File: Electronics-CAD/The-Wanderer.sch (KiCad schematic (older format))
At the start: 9 parts, among them J1 Raspberry_Pi_3, M1_Left Continuous_Motor_Servo, M2_Right Continuous_Motor_Servo, U1 IR_sensor

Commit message: Fix schematic by replacing voltage divider with voltage converter
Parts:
- removed RN2: Voltage_Divider, symbol Device:Voltage_Divider
- added B1: 5V_2A_Voltage_Converter, symbol Raspberry_Pi_2_or_3:5V_2A_Voltage_Converter
- A1: symbol POE_Elias:Arduino_UNO_R3 -> The-Wanderer-rescue:Arduino_UNO_R3-POE_Elias
- J1: symbol Raspberry_Pi_2_or_3:Raspberry_Pi_3 -> The-Wanderer-rescue:Raspberry_Pi_3-Raspberry_Pi_2_or_3
- LS1: symbol Raspberry_Pi_2_or_3:Raspi_Speaker -> The-Wanderer-rescue:Raspi_Speaker-Raspberry_Pi_2_or_3
- U1: symbol Raspberry_Pi_2_or_3:IR_sensor -> The-Wanderer-rescue:IR_sensor-Raspberry_Pi_2_or_3
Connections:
- net 12V: now also B1.~
- net 5V: now also B1.~
- net GND: now also B1.~
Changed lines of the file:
@@
 $EndComp
 $Comp
-L Raspberry_Pi_2_or_3:IR_sensor U1
+L The-Wanderer-rescue:IR_sensor-Raspberry_Pi_2_or_3 U1
 U 1 1 5DF263DA
 P 3650 2350
@@
 	2200 2650 2250 2650
 $Comp
-L Device:Voltage_Divider RN2
-U 1 1 5DF46FB6
-P 4100 1500
-F 0 "RN2" V 3900 1500 50  0000 C CNN
-F 1 "Voltage_Divider" V 4000 1500 50  0000 C CNN
-F 2 "" V 4575 1500 50  0001 C CNN
-F 3 "~" H 4300 1500 50  0001 C CNN
-	1    4100 1500
-	0    1    -1   0
-$EndComp
-Text Label 4100 1200 3    50   ~ 0
-5V
-$Comp
 L power:GND #PWR?
 U 1 1 5DF4FBFA
@@
 $EndComp
 $Comp
-L Raspberry_Pi_2_or_3:Raspi_Speaker LS1
+L The-Wanderer-rescue:Raspi_Speaker-Raspberry_Pi_2_or_3 LS1
 U 1 1 5DF1BB42
 P 4400 3250
@@
 $EndComp
 $Comp
-L Raspberry_Pi_2_or_3:Raspberry_Pi_3 J1
+L The-Wanderer-rescue:Raspberry_Pi_3-Raspberry_Pi_2_or_3 J1
 U 1 1 5DF103EF
 P 5400 2450
@@
 	5200 1150 5200 900
 Wire Wire Line
-	5200 900  4100 900
-Wire Wire Line
-	4100 900  4100 1350
-Connection ~ 4100 900
-Wire Wire Line
-	2700 900  4100 900
-Wire Wire Line
 	3400 2650 3400 1350
 Wire Wire Line
@@
 	2700 1350 2700 1400
 Wire Wire Line
-	3850 1500 3850 1300
-Wire Wire Line
 	4450 1000 4450 1050
-Wire Wire Line
-	3850 1000 4350 1000
-Wire Wire Line
-	4350 1000 4350 1500
-Connection ~ 4350 1000
-Wire Wire Line
-	4350 1000 4450 1000
-Text Label 3850 1450 1    50   ~ 0
+Text Label 4050 1300 2    50   ~ 0
 12V
 Text Label 4100 900  0    50   ~ 0
@@
 	2050 2700 2050 1300
 $Comp
-L POE_Elias:Arduino_UNO_R3 A1
+L The-Wanderer-rescue:Arduino_UNO_R3-POE_Elias A1
 U 1 1 5DEEA028
 P 2800 2450
@@
 Wire Wire Line
 	3450 3450 3450 2400
+$Comp
+L Raspberry_Pi_2_or_3:5V_2A_Voltage_Converter B1
+U 1 1 5DF0F40C
+P 4300 1500
+F 0 "B1" V 4350 1500 50  0000 R CNN
+F 1 "5V_2A_Voltage_Converter" V 4450 2150 50  0000 R CNN
+F 2 "" H 4300 1500 50  0001 C CNN
+F 3 "" H 4300 1500 50  0001 C CNN
+	1    4300 1500
+	0    -1   1    0
+$EndComp
+Wire Wire Line
+	3850 1000 4150 1000
+Wire Wire Line
+	4150 1300 4150 1000
+Connection ~ 4150 1000
+Wire Wire Line
+	4150 1000 4450 1000
+Wire Wire Line
+	4200 1300 4200 900
+Wire Wire Line
+	2700 900  4200 900
+Connection ~ 4200 900
+Wire Wire Line
+	4200 900  5200 900
+Wire Wire Line
+	4050 1300 3850 1300
 $EndSCHEMATC

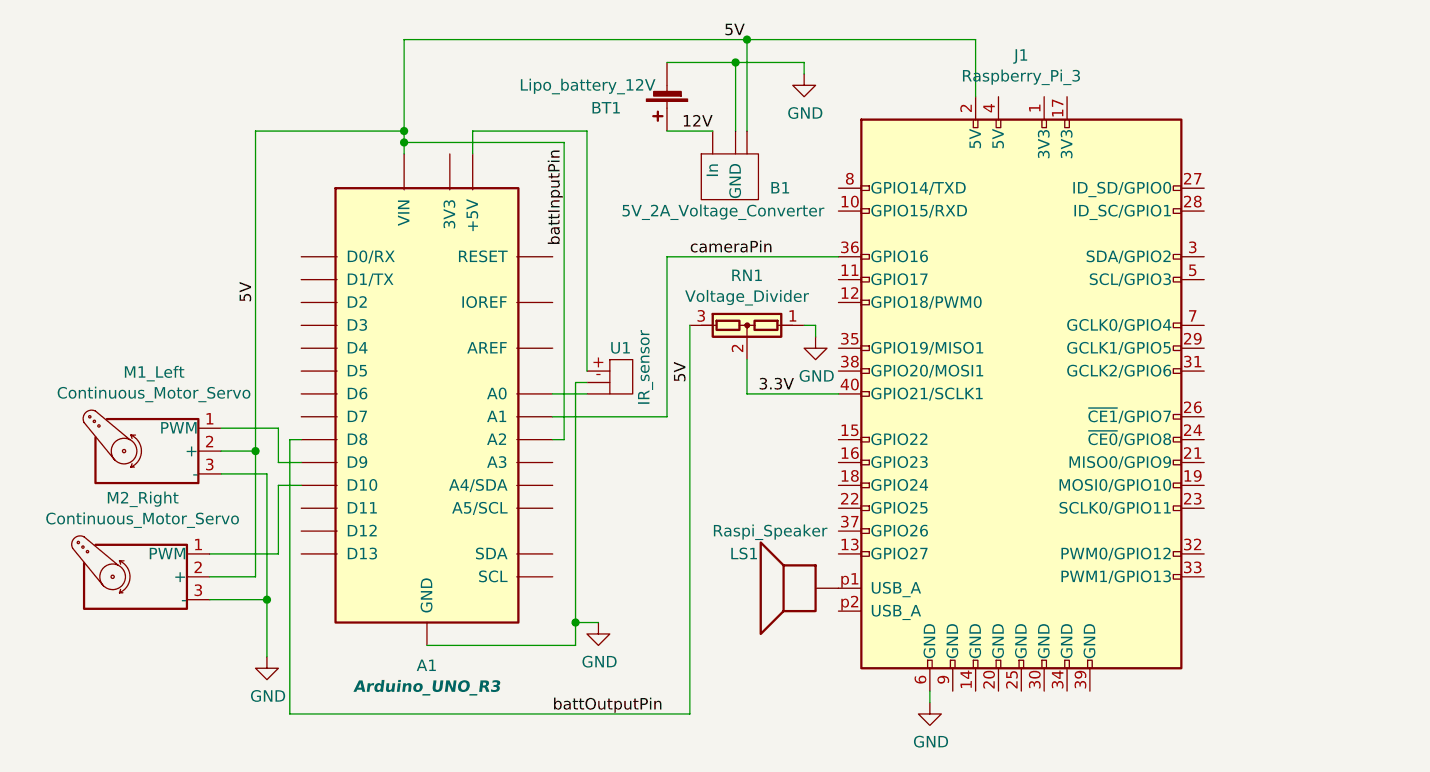
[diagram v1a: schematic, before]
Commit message: Add voltage divider from battery to battInputPin
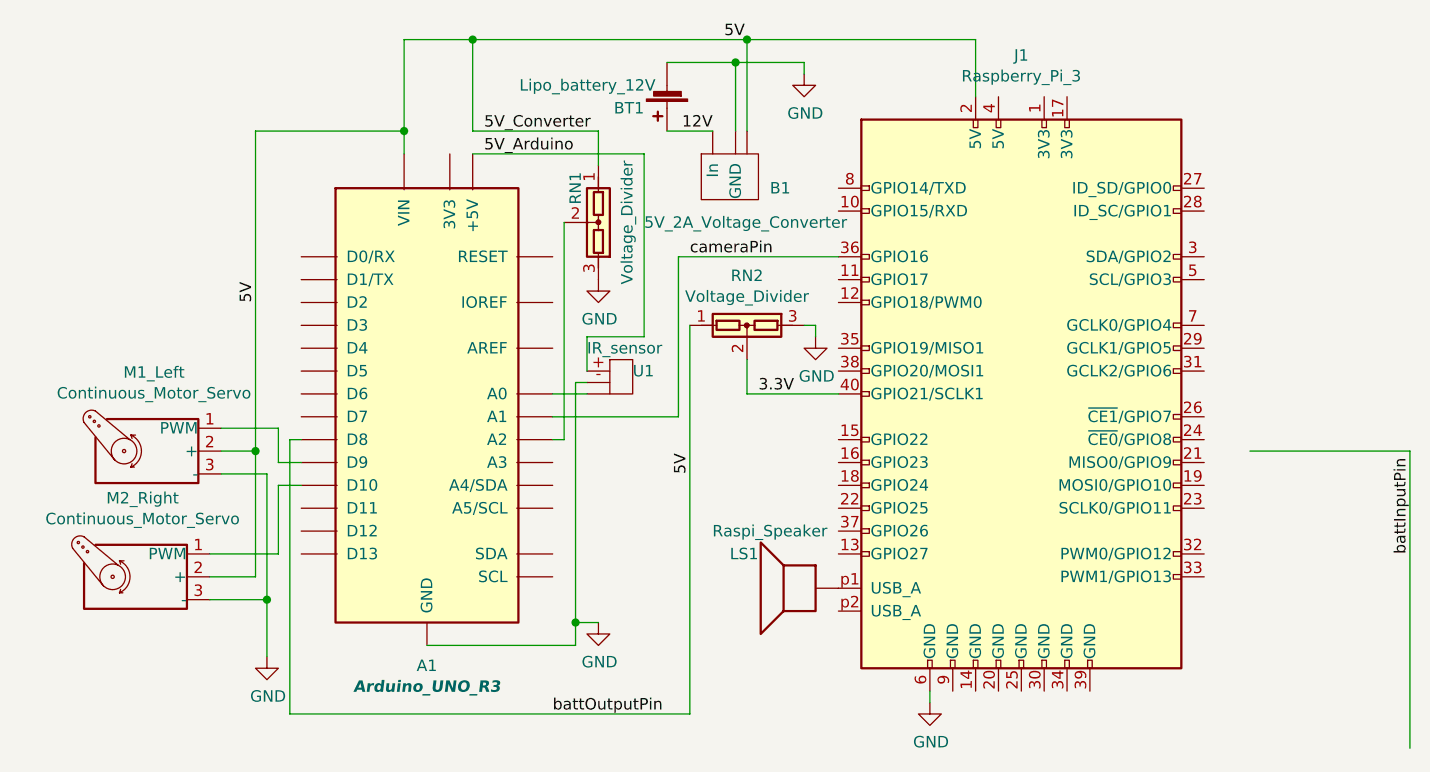
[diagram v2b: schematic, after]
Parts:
- added RN1: Voltage_Divider, symbol Device:Voltage_Divider
- renumbered RN1 to RN2
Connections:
- net labels added: 5V_Arduino, 5V_Converter
- wire segments 51 -> 56
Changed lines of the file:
@@
 Sheet 1 1
 Title "The Wanderer Circuit"
-Date "2019-12-09"
+Date "2019-13-09"
 Rev ""
 Comp "Case Zito"
@@
 U 1 1 5DF263DA
 P 3650 2350
-F 0 "U1" H 3600 2450 50  0000 L CNN
-F 1 "IR_sensor" V 3750 2200 50  0000 L CNN
+F 0 "U1" H 3700 2350 50  0000 L CNN
+F 1 "IR_sensor" H 3500 2450 50  0000 L CNN
 F 2 "" H 3650 2450 50  0001 C CNN
 F 3 "" H 3650 2450 50  0001 C CNN
@@
 Wire Wire Line
 	1900 2600 2150 2600
-$Comp
-L Device:Battery_Cell BT1
-U 1 1 5DF2AE3F
-P 3850 1100
-F 0 "BT1" H 4050 1200 50  0000 L CNN
-F 1 "Lipo_battery_12V" H 3900 1100 50  0000 L CNN
-F 2 "" V 3850 1160 50  0001 C CNN
-F 3 "~" V 3850 1160 50  0001 C CNN
-	1    3850 1100
-	-1   0    0    1
-$EndComp
 Wire Wire Line
 	2200 2650 2250 2650
@@
 Wire Wire Line
 	2150 2850 2150 3150
-Text Label 3950 2400 1    50   ~ 0
+Text Label 3950 2800 1    50   ~ 0
 5V
 Text Label 4250 2450 0    50   ~ 0
@@
 	4200 2300 4200 2450
 Wire Wire Line
-	3950 2150 3950 3850
-Wire Wire Line
 	4500 2150 4500 2200
 Wire Wire Line
 	4450 2150 4500 2150
 $Comp
-L Device:Voltage_Divider RN1
+L Device:Voltage_Divider RN2
 U 1 1 5DF3DF89
 P 4200 2150
-F 0 "RN1" V 3983 2150 50  0000 C CNN
+F 0 "RN2" V 3983 2150 50  0000 C CNN
 F 1 "Voltage_Divider" V 4074 2150 50  0000 C CNN
 F 2 "" V 4675 2150 50  0001 C CNN
 F 3 "~" H 4400 2150 50  0001 C CNN
 	1    4200 2150
-	0    1    1    0
+	0    -1   1    0
 $EndComp
 $Comp
@@
 	3350 2650 3400 2650
 Wire Wire Line
-	3500 2350 3500 1300
-Wire Wire Line
-	3500 1300 3000 1300
-Wire Wire Line
-	3000 1300 3000 1400
-Wire Wire Line
 	2800 3550 3450 3550
 Wire Wire Line
@@
 	3450 2400 3500 2400
 Wire Wire Line
-	3350 2550 3850 2550
-Wire Wire Line
-	3850 2550 3850 1850
-Wire Wire Line
-	3850 1850 4600 1850
+	3900 2550 3900 1850
 Wire Wire Line
 	5200 1150 5200 900
 Wire Wire Line
-	3400 2650 3400 1350
-Wire Wire Line
-	3400 1350 2700 1350
+	7100 4000 7100 2700
+Wire Wire Line
+	7100 2700 6400 2700
 Wire Wire Line
 	2700 900  2700 1300
-Connection ~ 2700 1350
-Wire Wire Line
-	2700 1350 2700 1400
 Wire Wire Line
 	4450 1000 4450 1050
@@
 	1900 2700 2050 2700
 Connection ~ 2700 1300
-Wire Wire Line
-	2700 1300 2700 1350
 Wire Wire Line
 	1850 3250 2050 3250
@@
 Text Label 3950 1850 0    50   ~ 0
 cameraPin
-Text Label 3400 1800 1    50   ~ 0
+Text Label 7100 3150 1    50   ~ 0
 battInputPin
 $Comp
@@
 P 4300 1500
 F 0 "B1" V 4350 1500 50  0000 R CNN
-F 1 "5V_2A_Voltage_Converter" V 4450 2150 50  0000 R CNN
+F 1 "5V_2A_Voltage_Converter" V 4500 2050 50  0000 R CNN
 F 2 "" H 4300 1500 50  0001 C CNN
 F 3 "" H 4300 1500 50  0001 C CNN
@@
 	4200 1300 4200 900
 Wire Wire Line
-	2700 900  4200 900
+	2700 900  3000 900
 Connection ~ 4200 900
 Wire Wire Line
@@
 Wire Wire Line
 	4050 1300 3850 1300
+$Comp
+L power:GND #PWR?
+U 1 1 5DF40BC2
+P 3550 1950
+F 0 "#PWR?" H 3550 1700 50  0001 C CNN
+F 1 "GND" H 3555 1777 50  0000 C CNN
+F 2 "" H 3550 1950 50  0001 C CNN
+F 3 "" H 3550 1950 50  0001 C CNN
+	1    3550 1950
+	1    0    0    -1
+$EndComp
+Wire Wire Line
+	2700 1300 2700 1400
+Wire Wire Line
+	3550 1300 3550 1450
+Wire Wire Line
+	3500 2200 3500 2350
+Wire Wire Line
+	3400 1700 3400 2650
+Wire Wire Line
+	3000 1400 3750 1400
+Wire Wire Line
+	3550 1300 3000 1300
+Wire Wire Line
+	3000 1300 3000 900
+Connection ~ 3000 900
+Wire Wire Line
+	3000 900  4200 900
+Text Label 3050 1400 0    50   ~ 0
+5V_Arduino
+Text Label 3050 1300 0    50   ~ 0
+5V_Converter
+$Comp
+L Device:Battery_Cell BT1
+U 1 1 5DF2AE3F
+P 3850 1100
+F 0 "BT1" H 3950 1200 50  0000 L CNN
+F 1 "Lipo_battery_12V" H 3900 1100 50  0000 L CNN
+F 2 "" V 3850 1160 50  0001 C CNN
+F 3 "~" V 3850 1160 50  0001 C CNN
+	1    3850 1100
+	-1   0    0    1
+$EndComp
+$Comp
+L Device:Voltage_Divider RN1
+U 1 1 5DF40BBC
+P 3550 1700
+F 0 "RN1" V 3650 1850 50  0000 C CNN
+F 1 "Voltage_Divider" V 3424 1700 50  0000 C CNN
+F 2 "" V 4025 1700 50  0001 C CNN
+F 3 "~" H 3750 1700 50  0001 C CNN
+	1    3550 1700
+	-1   0    0    -1
+$EndComp
+Wire Wire Line
+	3500 2200 3750 2200
+Wire Wire Line
+	3750 1400 3750 2200
+Wire Wire Line
+	3950 2150 3950 3850
+Wire Wire Line
+	3900 1850 4600 1850
+Wire Wire Line
+	3350 2550 3900 2550
 $EndSCHEMATC

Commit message: Add voltage divider for battInputPin (actual)
The commit before this was not successful
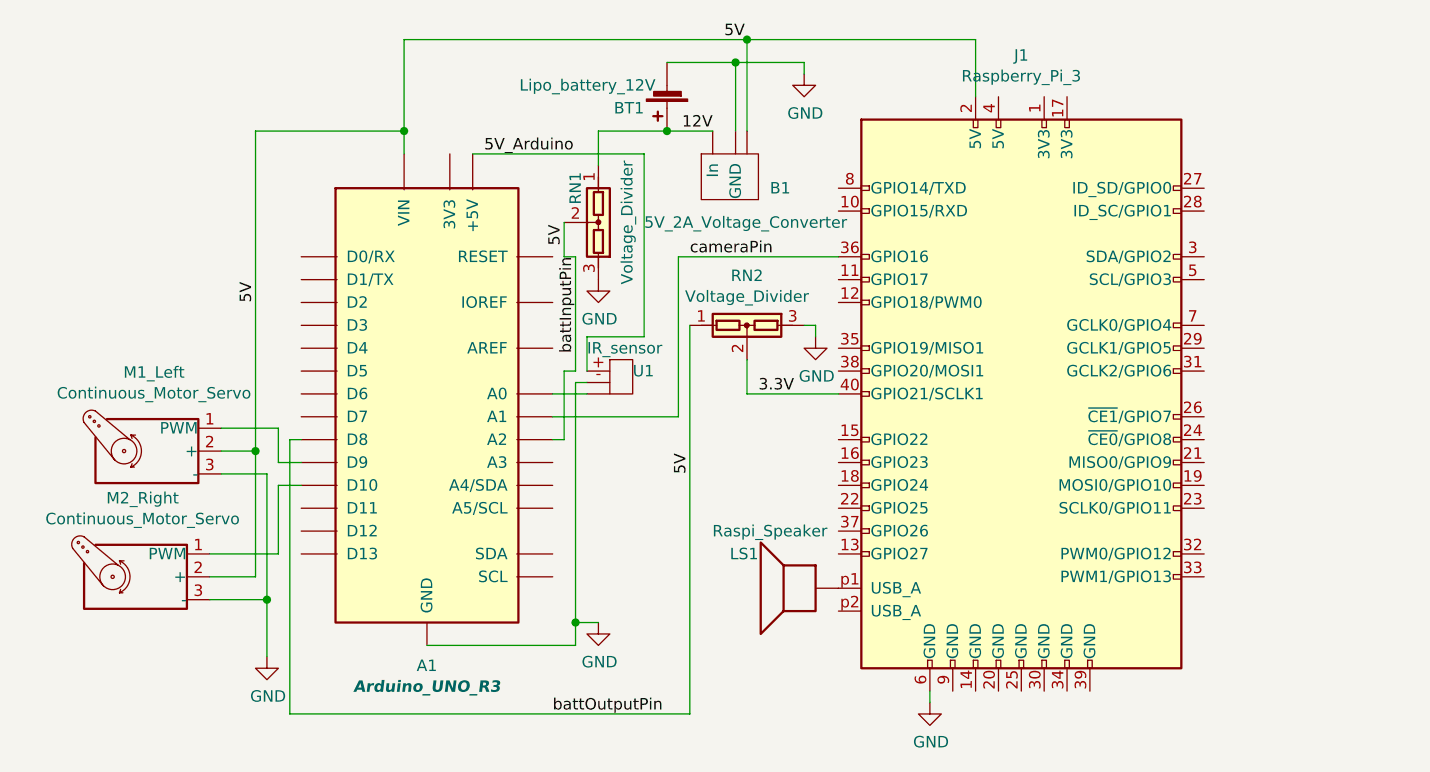
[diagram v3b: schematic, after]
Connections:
- net labels removed: 5V_Converter
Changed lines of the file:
@@
 	5200 1150 5200 900
-Wire Wire Line
-	7100 4000 7100 2700
-Wire Wire Line
-	7100 2700 6400 2700
 Wire Wire Line
 	2700 900  2700 1300
@@
 Text Label 3950 1850 0    50   ~ 0
 cameraPin
-Text Label 7100 3150 1    50   ~ 0
+Text Label 3450 1850 3    50   ~ 0
 battInputPin
 $Comp
@@
 Wire Wire Line
 	4200 1300 4200 900
-Wire Wire Line
-	2700 900  3000 900
 Connection ~ 4200 900
 Wire Wire Line
@@
 	3500 2200 3500 2350
 Wire Wire Line
-	3400 1700 3400 2650
-Wire Wire Line
 	3000 1400 3750 1400
-Wire Wire Line
-	3550 1300 3000 1300
-Wire Wire Line
-	3000 1300 3000 900
-Connection ~ 3000 900
-Wire Wire Line
-	3000 900  4200 900
 Text Label 3050 1400 0    50   ~ 0
 5V_Arduino
-Text Label 3050 1300 0    50   ~ 0
-5V_Converter
 $Comp
 L Device:Battery_Cell BT1
@@
 Wire Wire Line
 	3350 2550 3900 2550
+Wire Wire Line
+	3550 1300 3850 1300
+Connection ~ 3850 1300
+Wire Wire Line
+	2700 900  4200 900
+Text Label 3400 1800 1    50   ~ 0
+5V
+Wire Wire Line
+	3400 1700 3400 1850
+Wire Wire Line
+	3400 1850 3450 1850
+Wire Wire Line
+	3450 1850 3450 2350
+Wire Wire Line
+	3450 2350 3400 2350
+Wire Wire Line
+	3400 2350 3400 2650
 $EndSCHEMATC
